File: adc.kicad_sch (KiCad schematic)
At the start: 9 parts, among them U701 AD7357xRU

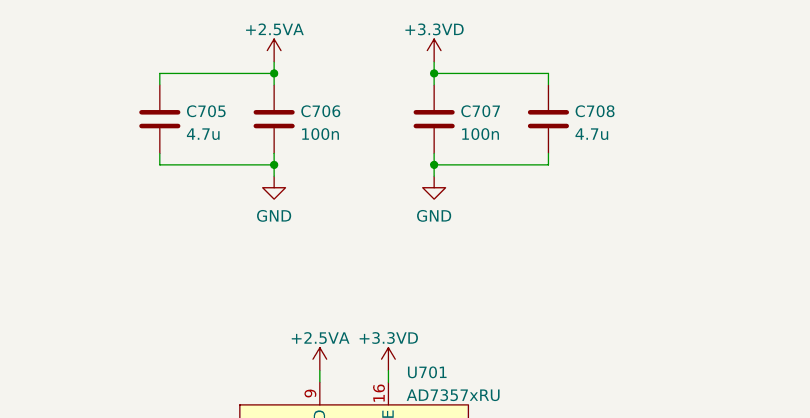
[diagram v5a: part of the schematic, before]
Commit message: Update schematic: - Redesign of decoupling based on swcad modelling (predominantly use 1uf, no paralleled caps) - Reroute REF_CLK_IN, CLK_SEL net to different FPGA pins - Some net renaming - Ext conn: add decoupling to 3v3 output - Reassign references to all components PCB: routing almost finished
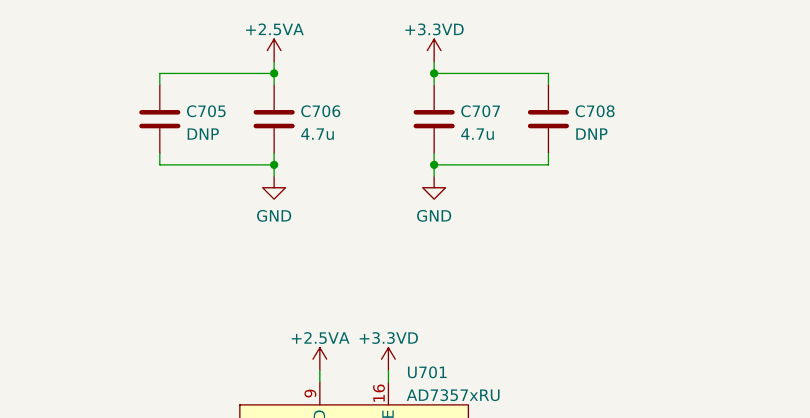
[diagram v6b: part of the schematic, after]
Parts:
- C705: renamed from C706; value 100n -> DNP; Mfr Samsung -> (none); Mfr PN CL21B104KBFNNNE -> (none)
- C708: renamed from C707; value 100n -> DNP; Mfr Samsung -> (none); Mfr PN CL21B104KBFNNNE -> (none)
- renumbered C705 to C706, C708 to C707
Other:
- moved on the sheet: C705, C706, C707, C708
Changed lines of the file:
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@@
     (pin "1")
   )
-  (symbol (lib_id "Device:C") (at 149.86 44.45 0) (unit 1)
-    (in_bom yes) (on_board yes) (fields_autoplaced)
-    (property "Reference" "C706" (id 0) (at 152.781 43.6153 0)
-      (effects (font (size 1.27 1.27)) (justify left))
-    )
-    (property "Value" "100n" (id 1) (at 152.781 46.1522 0)
-      (effects (font (size 1.27 1.27)) (justify left))
-    )
-    (property "Footprint" "Capacitor_SMD:C_0805_2012Metric" (id 2) (at 150.8252 48.26 0)
-      (effects (font (size 1.27 1.27)) hide)
-    )
-    (property "Datasheet" "~" (id 3) (at 149.86 44.45 0)
-      (effects (font (size 1.27 1.27)) hide)
-    )
-    (property "Spec1" "" (id 4) (at 149.86 44.45 0)
-      (effects (font (size 1.27 1.27)) hide)
-    )
-    (property "Spec2" "" (id 5) (at 149.86 44.45 0)
-      (effects (font (size 1.27 1.27)) hide)
-    )
-    (property "Tolerance" "" (id 6) (at 149.86 44.45 0)
-      (effects (font (size 1.27 1.27)) hide)
-    )
-    (property "Mfr" "Samsung" (id 7) (at 149.86 44.45 0)
-      (effects (font (size 1.27 1.27)) hide)
-    )
-    (property "Mfr PN" "CL21B104KBFNNNE" (id 8) (at 149.86 44.45 0)
+  (symbol (lib_id "Device:C") (at 137.16 44.45 0) (unit 1)
+    (in_bom yes) (on_board yes) (fields_autoplaced)
+    (property "Reference" "C705" (id 0) (at 140.081 43.6153 0)
+      (effects (font (size 1.27 1.27)) (justify left))
+    )
+    (property "Value" "DNP" (id 1) (at 140.081 46.1522 0)
+      (effects (font (size 1.27 1.27)) (justify left))
+    )
+    (property "Footprint" "Capacitor_SMD:C_0805_2012Metric" (id 2) (at 138.1252 48.26 0)
+      (effects (font (size 1.27 1.27)) hide)
+    )
+    (property "Datasheet" "~" (id 3) (at 137.16 44.45 0)
       (effects (font (size 1.27 1.27)) hide)
     )
@@
     (pin "1")
   )
+  (symbol (lib_id "Device:C") (at 167.64 44.45 0) (unit 1)
+    (in_bom yes) (on_board yes) (fields_autoplaced)
+    (property "Reference" "C707" (id 0) (at 170.561 43.6153 0)
+      (effects (font (size 1.27 1.27)) (justify left))
+    )
+    (property "Value" "4.7u" (id 1) (at 170.561 46.1522 0)
+      (effects (font (size 1.27 1.27)) (justify left))
+    )
+    (property "Footprint" "Capacitor_SMD:C_0805_2012Metric" (id 2) (at 168.6052 48.26 0)
+      (effects (font (size 1.27 1.27)) hide)
+    )
+    (property "Datasheet" "~" (id 3) (at 167.64 44.45 0)
+      (effects (font (size 1.27 1.27)) hide)
+    )
+    (property "Spec1" "" (id 4) (at 167.64 44.45 0)
+      (effects (font (size 1.27 1.27)) hide)
+    )
+    (property "Spec2" "" (id 5) (at 167.64 44.45 0)
+      (effects (font (size 1.27 1.27)) hide)
+    )
+    (property "Tolerance" "" (id 6) (at 167.64 44.45 0)
+      (effects (font (size 1.27 1.27)) hide)
+    )
+    (property "Mfr" "Murata" (id 7) (at 167.64 44.45 0)
+      (effects (font (size 1.27 1.27)) hide)
+    )
+    (property "Mfr PN" "GRM21BR71C475ME51" (id 8) (at 167.64 44.45 0)
+      (effects (font (size 1.27 1.27)) hide)
+    )
+    (pin "1")
+    (pin "2")
+  )
   (symbol (lib_id "Device:C") (at 180.34 44.45 0) (unit 1)
     (in_bom yes) (on_board yes) (fields_autoplaced)
@@
       (effects (font (size 1.27 1.27)) (justify left))
     )
-    (property "Value" "4.7u" (id 1) (at 183.261 46.1522 0)
+    (property "Value" "DNP" (id 1) (at 183.261 46.1522 0)
       (effects (font (size 1.27 1.27)) (justify left))
     )
@@
       (effects (font (size 1.27 1.27)) hide)
     )
-    (property "Spec1" "" (id 4) (at 180.34 44.45 0)
-      (effects (font (size 1.27 1.27)) hide)
-    )
-    (property "Spec2" "" (id 5) (at 180.34 44.45 0)
-      (effects (font (size 1.27 1.27)) hide)
-    )
-    (property "Tolerance" "" (id 6) (at 180.34 44.45 0)
-      (effects (font (size 1.27 1.27)) hide)
-    )
-    (property "Mfr" "Murata" (id 7) (at 180.34 44.45 0)
-      (effects (font (size 1.27 1.27)) hide)
-    )
-    (property "Mfr PN" "GRM21BR71C475ME51" (id 8) (at 180.34 44.45 0)
-      (effects (font (size 1.27 1.27)) hide)
-    )
-    (pin "1")
-    (pin "2")
-  )
-  (symbol (lib_id "Device:C") (at 167.64 44.45 0) (unit 1)
-    (in_bom yes) (on_board yes) (fields_autoplaced)
-    (property "Reference" "C707" (id 0) (at 170.561 43.6153 0)
-      (effects (font (size 1.27 1.27)) (justify left))
-    )
-    (property "Value" "100n" (id 1) (at 170.561 46.1522 0)
-      (effects (font (size 1.27 1.27)) (justify left))
-    )
-    (property "Footprint" "Capacitor_SMD:C_0805_2012Metric" (id 2) (at 168.6052 48.26 0)
-      (effects (font (size 1.27 1.27)) hide)
-    )
-    (property "Datasheet" "~" (id 3) (at 167.64 44.45 0)
-      (effects (font (size 1.27 1.27)) hide)
-    )
-    (property "Spec1" "" (id 4) (at 167.64 44.45 0)
-      (effects (font (size 1.27 1.27)) hide)
-    )
-    (property "Spec2" "" (id 5) (at 167.64 44.45 0)
-      (effects (font (size 1.27 1.27)) hide)
-    )
-    (property "Tolerance" "" (id 6) (at 167.64 44.45 0)
-      (effects (font (size 1.27 1.27)) hide)
-    )
-    (property "Mfr" "Samsung" (id 7) (at 167.64 44.45 0)
-      (effects (font (size 1.27 1.27)) hide)
-    )
-    (property "Mfr PN" "CL21B104KBFNNNE" (id 8) (at 167.64 44.45 0)
-      (effects (font (size 1.27 1.27)) hide)
-    )
-    (pin "1")
-    (pin "2")
-  )
-  (symbol (lib_id "Device:C") (at 137.16 44.45 0) (unit 1)
-    (in_bom yes) (on_board yes) (fields_autoplaced)
-    (property "Reference" "C705" (id 0) (at 140.081 43.6153 0)
-      (effects (font (size 1.27 1.27)) (justify left))
-    )
-    (property "Value" "4.7u" (id 1) (at 140.081 46.1522 0)
-      (effects (font (size 1.27 1.27)) (justify left))
-    )
-    (property "Footprint" "Capacitor_SMD:C_0805_2012Metric" (id 2) (at 138.1252 48.26 0)
-      (effects (font (size 1.27 1.27)) hide)
-    )
-    (property "Datasheet" "~" (id 3) (at 137.16 44.45 0)
-      (effects (font (size 1.27 1.27)) hide)
-    )
-    (property "Spec1" "" (id 4) (at 137.16 44.45 0)
-      (effects (font (size 1.27 1.27)) hide)
-    )
-    (property "Spec2" "" (id 5) (at 137.16 44.45 0)
-      (effects (font (size 1.27 1.27)) hide)
-    )
-    (property "Tolerance" "" (id 6) (at 137.16 44.45 0)
-      (effects (font (size 1.27 1.27)) hide)
-    )
-    (property "Mfr" "Murata" (id 7) (at 137.16 44.45 0)
-      (effects (font (size 1.27 1.27)) hide)
-    )
-    (property "Mfr PN" "GRM21BR71C475ME51" (id 8) (at 137.16 44.45 0)
-      (effects (font (size 1.27 1.27)) hide)
-    )
+    (pin "1")
+    (pin "2")
+  )
+  (symbol (lib_id "Device:C") (at 149.86 44.45 0) (unit 1)
+    (in_bom yes) (on_board yes) (fields_autoplaced)
+    (property "Reference" "C706" (id 0) (at 152.781 43.6153 0)
+      (effects (font (size 1.27 1.27)) (justify left))
+    )
+    (property "Value" "4.7u" (id 1) (at 152.781 46.1522 0)
+      (effects (font (size 1.27 1.27)) (justify left))
+    )
+    (property "Footprint" "Capacitor_SMD:C_0805_2012Metric" (id 2) (at 150.8252 48.26 0)
+      (effects (font (size 1.27 1.27)) hide)
+    )
+    (property "Datasheet" "~" (id 3) (at 149.86 44.45 0)
+      (effects (font (size 1.27 1.27)) hide)
+    )
+    (property "Spec1" "" (id 4) (at 149.86 44.45 0)
+      (effects (font (size 1.27 1.27)) hide)
+    )
+    (property "Spec2" "" (id 5) (at 149.86 44.45 0)
+      (effects (font (size 1.27 1.27)) hide)
+    )
+    (property "Tolerance" "" (id 6) (at 149.86 44.45 0)
+      (effects (font (size 1.27 1.27)) hide)
+    )
+    (property "Mfr" "Murata" (id 7) (at 149.86 44.45 0)
+      (effects (font (size 1.27 1.27)) hide)
+    )
+    (property "Mfr PN" "GRM21BR71C475ME51" (id 8) (at 149.86 44.45 0)
+      (effects (font (size 1.27 1.27)) hide)
+    )
